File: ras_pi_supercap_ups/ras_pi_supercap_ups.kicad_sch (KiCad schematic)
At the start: 58 parts, among them J1 Conn_01x03, J2 Conn_02x03_Odd_Even, J3 Conn_01x04, J4 Conn_01x04, J5 Conn_01x05, J6 Conn_01x05, J7 Barrel_Jack_Switch_Pin3Ring, Q1 SUD50P04-08, U1 ATtiny85-20P, U2 TL431LP, U3 TL431LP, U4 TL431LP, U5 TL431LP, U6 TL431LP, U7 LM2596S-5

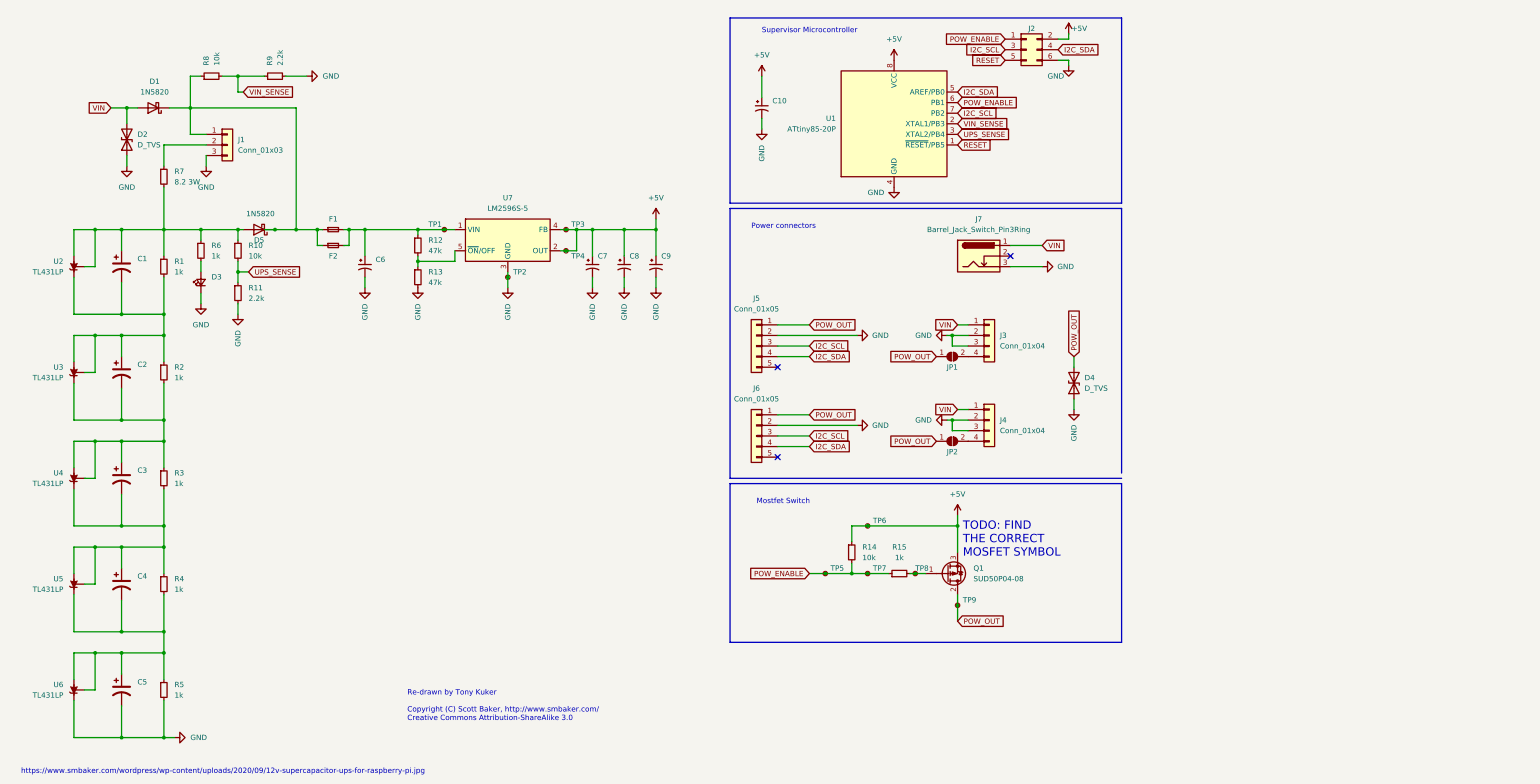
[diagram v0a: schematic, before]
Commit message: Updated part numbers
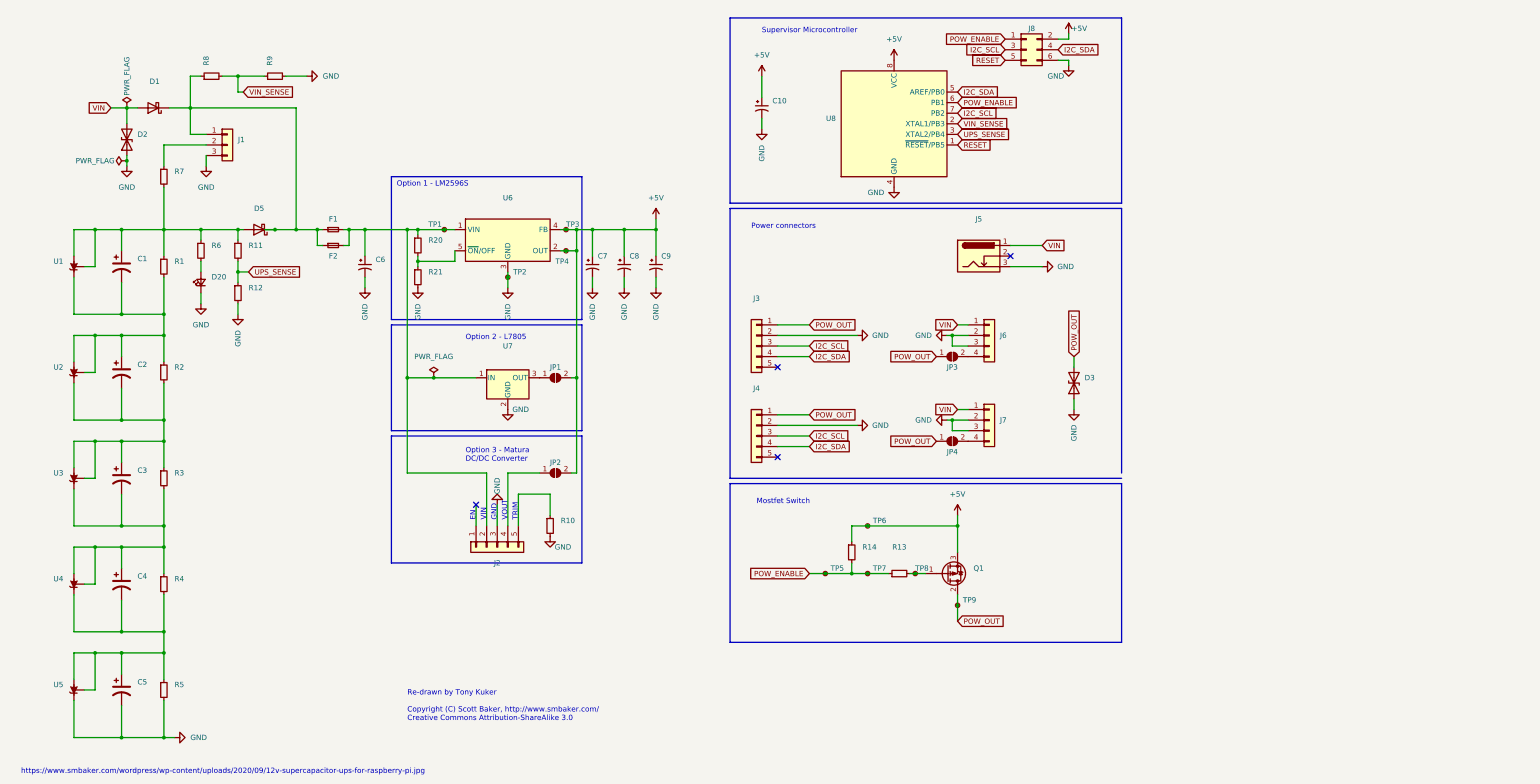
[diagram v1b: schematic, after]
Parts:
- added J2: (no value), symbol Connector_Generic:Conn_01x05
- added JP1, JP2: (no value), symbol Jumper:SolderJumper_2_Open
- added R10: (no value), symbol Device:R_Small
- added U7: (no value), symbol Regulator_Linear:L7805
- C1, C2, C3, C4, C5: value C_Polarized_US -> (none); DigikeyPN (none) -> 478-10996-ND
- C10, C7, C8, C9: value C_Polarized_Small_US -> (none); DigikeyPN (none) -> 445-173294-1-ND
- C6: value C_Polarized_Small_US -> (none); DigikeyPN (none) -> 445-FK26X7R1E106K-ND
- D1, D5: value 1N5820 -> (none); footprint Diode_THT:D_DO-201AD_P15.24mm_Horizontal -> (none); DigikeyPN (none) -> 1N5820-TPMSCT-ND; LCSC (none) -> C95400
- D2: value D_TVS -> (none); DigikeyPN (none) -> SA12ALFTR-ND
- D20: renamed from D3; value LED_Small -> (none); DigikeyPN (none) -> 67-2288-ND
- D3: renamed from D4; value D_TVS -> (none); DigikeyPN (none) -> SA12ALFTR-ND
- F1, F2: value Fuse_Small -> (none); DigikeyPN (none) -> F2315-ND; LCSC (none) -> C140540
- J1: value Conn_01x03 -> (none); footprint Connector_PinHeader_2.54mm:PinHeader_1x03_P2.54mm_Vertical -> (none); DigikeyPN (none) -> NA
- J3: renamed from J5; value Conn_01x05 -> (none); footprint Connector_PinHeader_2.54mm:PinHeader_1x05_P2.54mm_Vertical -> (none); DigikeyPN (none) -> NA
- J4: renamed from J6; value Conn_01x05 -> (none); footprint Connector_PinHeader_2.54mm:PinHeader_1x05_P2.54mm_Vertical -> (none); DigikeyPN (none) -> NA
- J5: renamed from J7; value Barrel_Jack_Switch_Pin3Ring -> (none); footprint Connector_BarrelJack:BarrelJack_CUI_PJ-063AH_Horizontal -> (none); DigikeyPN (none) -> NA
- J6: renamed from J3; value Conn_01x04 -> (none); footprint Connector_PinHeader_2.54mm:PinHeader_1x04_P2.54mm_Vertical -> (none); DigikeyPN (none) -> A106204-ND
- J7: renamed from J4; value Conn_01x04 -> (none); footprint Connector_PinHeader_2.54mm:PinHeader_1x04_P2.54mm_Vertical -> (none); DigikeyPN (none) -> A106204-ND
- J8: renamed from J2; value Conn_02x03_Odd_Even -> (none); DigikeyPN (none) -> NA
- JP3: renamed from JP1; value SolderJumper_2_Open -> (none); DigikeyPN (none) -> NA
- JP4: renamed from JP2; value SolderJumper_2_Open -> (none); DigikeyPN (none) -> NA
- Q1: value SUD50P04-08 -> (none); footprint Package_TO_SOT_SMD:TO-252-2 -> (none); DigikeyPN (none) -> IRF5305PBF-ND
- R1, R2, R3, R4, R5, R6: value 1k -> (none); DigikeyPN (none) -> CF14JT1K00CT-ND
- R11: renamed from R10; value 10k -> (none); DigikeyPN (none) -> CF14JT10K0CT-ND
- R12: renamed from R11; value 2.2k -> (none); DigikeyPN (none) -> CF14JT2K20TR-ND
- R13: renamed from R15; value 1k -> (none); DigikeyPN (none) -> CF14JT1K00CT-ND
- R14, R8: value 10k -> (none); DigikeyPN (none) -> CF14JT10K0CT-ND
- R20: renamed from R12; value 47k -> (none); DigikeyPN (none) -> CF14JT47K0TR-ND
- R21: renamed from R13; value 47k -> (none); DigikeyPN (none) -> CF14JT47K0TR-ND
- R7: value 8.2 3W -> (none); DigikeyPN (none) -> YAG1228CT-ND
- R9: value 2.2k -> (none); DigikeyPN (none) -> CF14JT2K20TR-ND
- TP1, TP2, TP3, TP4, TP5, TP6, TP7, TP8, TP9: value TestPoint_Small -> (none); DigikeyPN (none) -> N/A
- U1: renamed from U2; value TL431LP -> (none); footprint Package_TO_SOT_THT:TO-92_Inline -> (none); DigikeyPN (none) -> KA431AZTACT-ND; LCSC (none) -> C124501
- U2: renamed from U3; value TL431LP -> (none); footprint Package_TO_SOT_THT:TO-92_Inline -> (none); DigikeyPN (none) -> KA431AZTACT-ND; LCSC (none) -> C124501
- U3: renamed from U4; value TL431LP -> (none); footprint Package_TO_SOT_THT:TO-92_Inline -> (none); DigikeyPN (none) -> KA431AZTACT-ND; LCSC (none) -> C124501
- U4: renamed from U5; value TL431LP -> (none); footprint Package_TO_SOT_THT:TO-92_Inline -> (none); DigikeyPN (none) -> KA431AZTACT-ND; LCSC (none) -> C124501
- U5: renamed from U6; value TL431LP -> (none); footprint Package_TO_SOT_THT:TO-92_Inline -> (none); DigikeyPN (none) -> KA431AZTACT-ND; LCSC (none) -> C124501
- U6: renamed from U7; value LM2596S-5 -> (none); footprint Package_TO_SOT_SMD:TO-263-5_TabPin3 -> (none); DigikeyPN (none) -> LM2596S-5.0-ND
- U8: renamed from U1; value ATtiny85-20P -> (none); footprint Package_DIP:DIP-8_W7.62mm -> (none); DigikeyPN (none) -> ATTINY85-20PU-ND
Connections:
- net +5V: now also JP1.2 (B), JP2.2 (B)
- net GND: now also J2.3 (Pin_3), R10.2, U7.2 (GND)
- net at C6.1, F1.2, F2.2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: now also J2.2 (Pin_2), U7.1 (IN)
- new net: J2.4 (Pin_4), JP2.1 (A)
- new net: JP1.1 (A), U7.3 (OUT)
- new net: J2.5 (Pin_5), R10.1
- no-connect marks 3 -> 4
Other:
- note added: "EN"
- note added: "GND"
- note added: "Option 1 - LM2596S"
- note added: "Option 2 - L7805"
- note added: "Option 3 - Matura DC/DC Converter"
- note added: "TRIM"
- note added: "VIN"
- note added: "VOUT"
- note removed: "TODO: FIND THE CORRECT MOSFET SYMBOL"

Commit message: Started updating to SMT
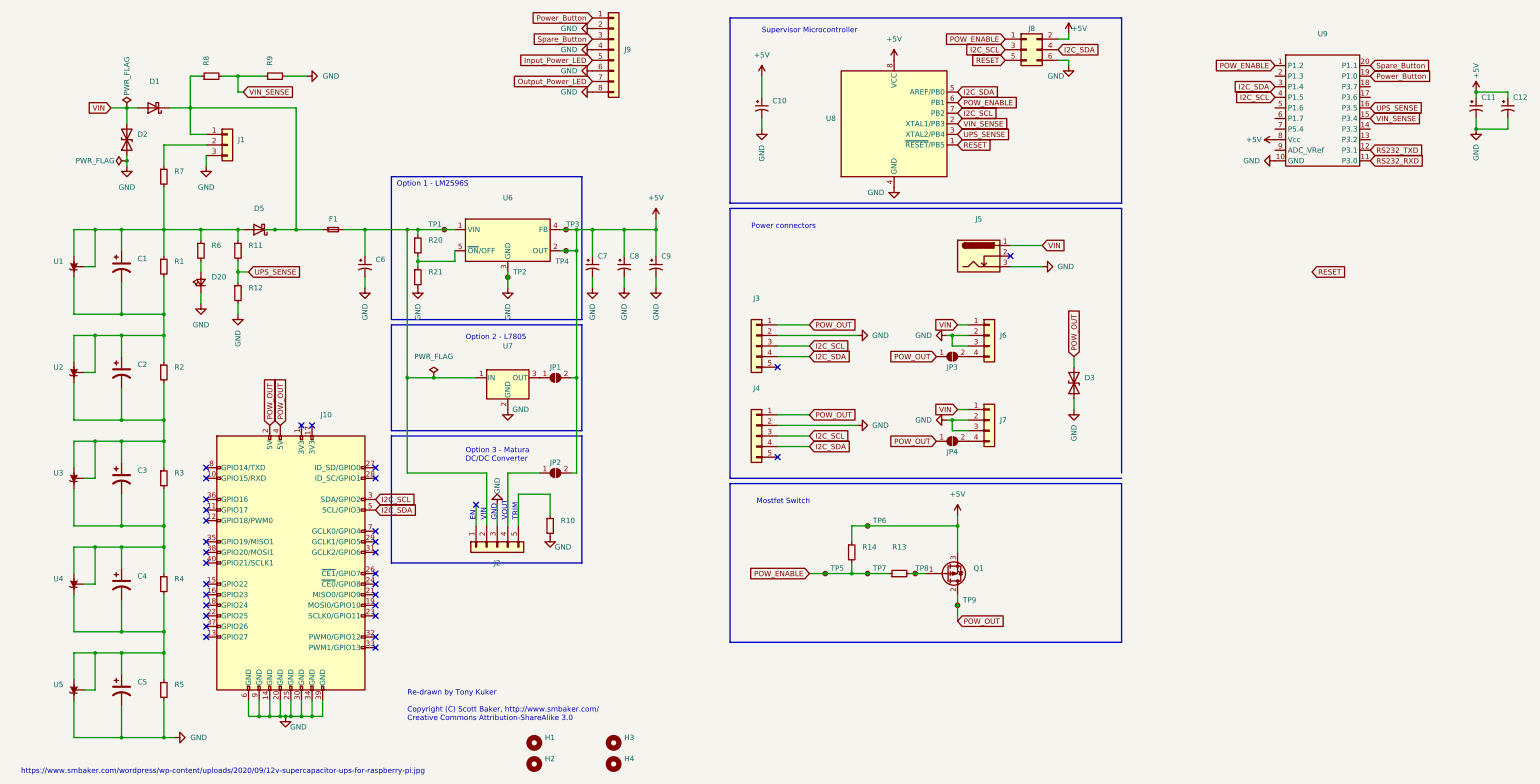
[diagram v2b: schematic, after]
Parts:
- removed F2: (no value), symbol Device:Fuse_Small
- added C11: 22u 10V X7R, Capacitor_SMD:C_0805_2012Metric, symbol Device:C_Polarized_Small_US
- added C12: (no value), symbol Device:C_Polarized_Small_US
- added H1, H2, H3, H4: (no value), symbol Mechanical:MountingHole
- added J10: (no value), symbol Connector:Raspberry_Pi_2_3
- added J9: (no value), symbol Connector_Generic:Conn_01x08
- added U9: (no value), symbol supercap_library:STC8H1K08
- D1, D5: DigikeyPN 1N5820-TPMSCT-ND -> (none); LCSC C95400 -> C17101
- D2, D3: DigikeyPN SA12ALFTR-ND -> (none); LCSC (none) -> C312234
- Q1: DigikeyPN IRF5305PBF-ND -> (none); LCSC (none) -> C878890
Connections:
- net +5V: now also C11.1, C12.1, U9.8 (Vcc)
- net GND: now also C11.2, C12.2, J10.14 (GND), J10.20 (GND), J10.25 (GND), J10.30 (GND), J10.34 (GND), J10.39 (GND), J10.6 (GND), J10.9 (GND), J9.2 (Pin_2), J9.4 (Pin_4), J9.6 (Pin_6), J9.8 (Pin_8), U9.10 (GND)
- net I2C_SCL: now also J10.3 (SDA/GPIO2), U9.4 (P1.5)
- net I2C_SDA: now also J10.5 (SCL/GPIO3), U9.3 (P1.4)
- net POW_ENABLE: now also U9.1 (P1.2)
- net POW_OUT: now also J10.2 (5V), J10.4 (5V)
- net UPS_SENSE: now also U9.16 (P3.5)
- net VIN_SENSE: now also U9.15 (P3.4)
- new net Input_Power_LED: J9.5 (Pin_5)
- new net Output_Power_LED: J9.7 (Pin_7)
- new net Power_Button: J9.1 (Pin_1), U9.19 (P1.0)
- new net RS232_RXD: U9.11 (P3.0)
- new net RS232_TXD: U9.12 (P3.1)
- new net Spare_Button: J9.3 (Pin_3), U9.20 (P1.1)
- no-connect marks 4 -> 32

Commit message: Updates
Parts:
- removed J10: (no value), symbol Connector:Raspberry_Pi_2_3
- removed J2: (no value), symbol Connector_Generic:Conn_01x05
- removed J5: (no value), symbol Connector:Barrel_Jack_Switch_Pin3Ring
- removed JP2: (no value), symbol Jumper:SolderJumper_2_Open
- removed R10: (no value), symbol Device:R_Small
- added J12: (no value), symbol 171826-4:171826-4
- C1, C2, C3, C4, C5: value (none) -> 10F; footprint (none) -> Capacitor_THT:CP_Radial_D12.5mm_P5.00mm
- C10, C7, C8, C9: value (none) -> 22u 10V X7R; footprint (none) -> Capacitor_SMD:C_0805_2012Metric
- C12: value (none) -> 0.1uF; footprint (none) -> Capacitor_SMD:C_0805_2012Metric
- C6: value (none) -> 10u 25V X7R; footprint (none) -> Capacitor_SMD:C_0805_2012Metric
- D1, D5: value (none) -> B340LA-13-F; footprint (none) -> Diode_SMD:D_SMA
- D2, D3: value (none) -> PTVSHC3D15VUH; footprint (none) -> Diode_SMD:D_SOD-323
- D20: value (none) -> Green; footprint (none) -> LED_SMD:LED_0805_2012Metric
- F1: value (none) -> Fuse_Small; footprint (none) -> Fuse:Fuse_1206_3216Metric
- H1, H2, H3, H4: value (none) -> MountingHole; footprint (none) -> MountingHole:MountingHole_2.7mm_M2.5
- J3, J4: value (none) -> Conn_01x05; footprint (none) -> Connector_PinHeader_2.54mm:PinHeader_1x05_P2.54mm_Vertical
- J6, J7: value (none) -> Conn_01x04; footprint (none) -> Connector_PinHeader_2.54mm:PinHeader_1x04_P2.54mm_Vertical
- J8: value (none) -> Conn_02x03_Odd_Even; footprint (none) -> Connector_PinHeader_2.54mm:PinHeader_2x03_P2.54mm_Vertical
- J9: value (none) -> LEDs and Buttons; footprint (none) -> Connector_PinHeader_2.54mm:PinHeader_1x08_P2.54mm_Vertical
- JP1, JP3, JP4: value (none) -> SolderJumper_2_Open; footprint (none) -> Jumper:SolderJumper-2_P1.3mm_Open_RoundedPad1.0x1.5mm
- Q1: value (none) -> IRF5305; footprint (none) -> Package_TO_SOT_SMD:TO-263-2
- R1, R2, R3, R4, R5: value (none) -> 1k; footprint (none) -> Resistor_SMD:R_1206_3216Metric
- R11, R14, R8: value (none) -> 10k; footprint (none) -> Resistor_SMD:R_0805_2012Metric
- R12, R9: value (none) -> 2.2k; footprint (none) -> Resistor_SMD:R_0805_2012Metric
- R13, R6: value (none) -> 1k; footprint (none) -> Resistor_SMD:R_0805_2012Metric
- R20, R21: value (none) -> 47k; footprint (none) -> Resistor_SMD:R_0805_2012Metric
- R7: value (none) -> 10 3W; footprint (none) -> Resistor_THT:R_Axial_DIN0516_L15.5mm_D5.0mm_P25.40mm_Horizontal
- TP1, TP2, TP3, TP4, TP5, TP6, TP7, TP8, TP9: value (none) -> TestPoint_Small; footprint (none) -> TestPoint:TestPoint_THTPad_D2.0mm_Drill1.0mm
- U1, U2, U3, U4, U5: value (none) -> KA431AZTA; footprint (none) -> Package_TO_SOT_THT:TO-92_Inline
- U6: value (none) -> LM2596S-5; footprint (none) -> Package_TO_SOT_SMD:TO-263-5_TabPin3
- U7: value (none) -> L7805; footprint (none) -> Package_TO_SOT_THT:TO-220-3_Vertical
- U8: value (none) -> ATtiny85-20P; footprint (none) -> Package_DIP:DIP-8_W7.62mm
- U9: value (none) -> STC8H1K08; footprint (none) -> Package_SO:TSSOP-20_4.4x5mm_P0.5mm
- renumbered J1 to J10
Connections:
- net GND: now also J12.2, J12.3
- net VIN: now also J12.1
- no-connect marks 32 -> 3
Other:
- added sheet Raspberry Pi Connectors (raspi_connectors.kicad_sch)
- note removed: "EN"
- note removed: "GND"
- note removed: "Option 3 - Matura DC/DC Converter"
- note removed: "TRIM"
- note removed: "VIN"
- note removed: "VOUT"
